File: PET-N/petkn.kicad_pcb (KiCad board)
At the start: 2 copper layers, 386.1 x 102 mm, 140 parts, among them J1 Extended_PET_keyboard_connect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, J4 AVR-ISP-6, J7 AVR-ISP-6, SW1 KP "=", SW10 KP "0", SW11 R SHIFT, SW12 ">", SW14 "]", SW15 "@", SW16 L SHIFT, SW17 KP "+", SW18 KP "2", SW2 KP ".", SW20 "?", SW21 ",", SW22 "N", SW23 "V", SW24 "X", SW25 KP "3", SW26 KP "1", SW27 RETURN, SW28 ";", SW29 "M", SW3 NC ($10), SW30 "B", SW31 "C", SW32 "Z", SW320 S LOCK, SW33 KP "*", SW34 KP "5", SW36 ":", SW37 "K", SW38 "H", SW39 "F", SW4 STOP, SW40 "S", SW41 KP "6", SW42 KP "4", SW44 "L", SW45 "J", SW46 "G", SW47 "D", SW48 "A", SW49 KP "/", SW5 "<", SW50 KP "8", SW52 "P", SW53 "I", SW54 "Y", SW55 "R", SW56 "W", SW57 KP "9", SW58 KP "7", SW59 U ARROW, SW6 SPACE, SW60 "O", SW61 "U", SW62 "T", SW63 "E", SW64 "Q", SW65 INS/DEL, SW66 UP/DOWN, SW67 NC ($0A), SW68 ")", SW69 "\", SW7 "[", SW70 "'", SW71 "$", SW72 QUOTE, SW73 LEFT/RIGHT, SW74 CLR/HOME, SW75 B ARROW, SW76 "(", SW77 "&", SW78 "%", SW79 "#", SW8 OFF/RVS, SW80 "!", SW9 KP "-", U1 LSF0204Q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

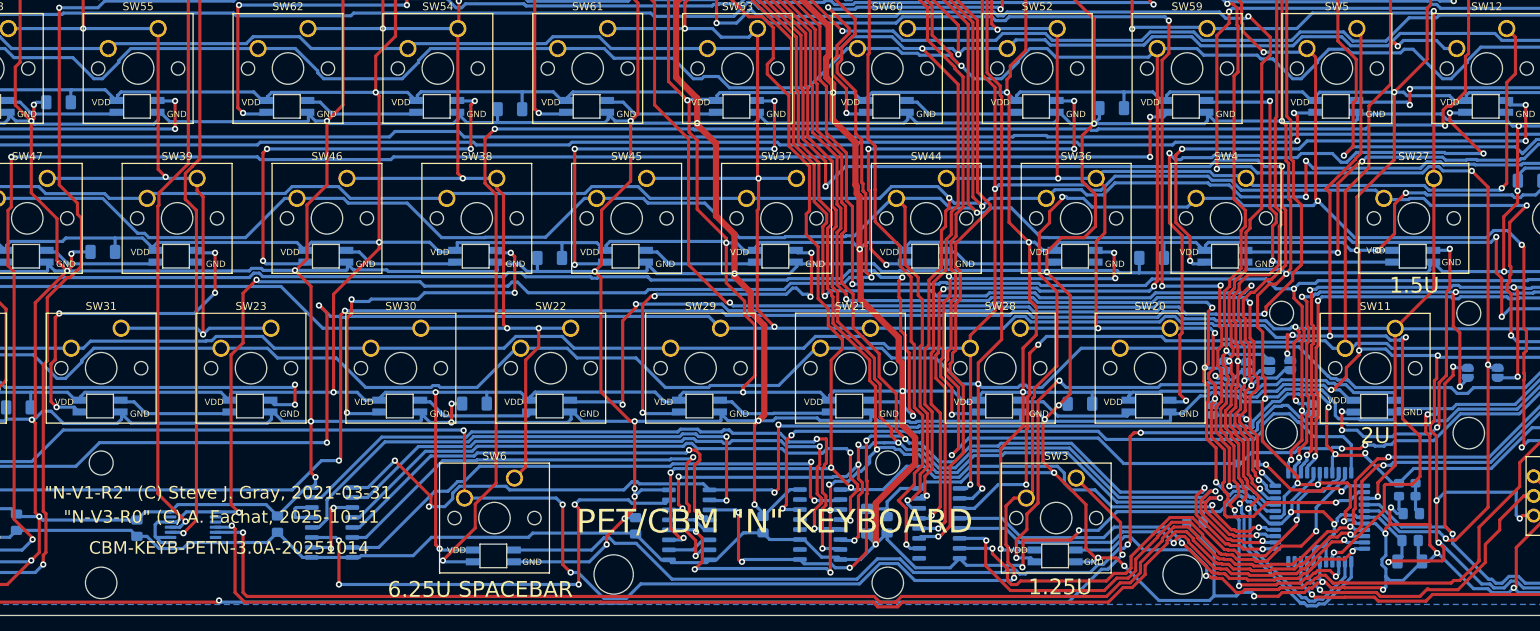
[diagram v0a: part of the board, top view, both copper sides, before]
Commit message: fix the two 3.0A issues (temporarily)
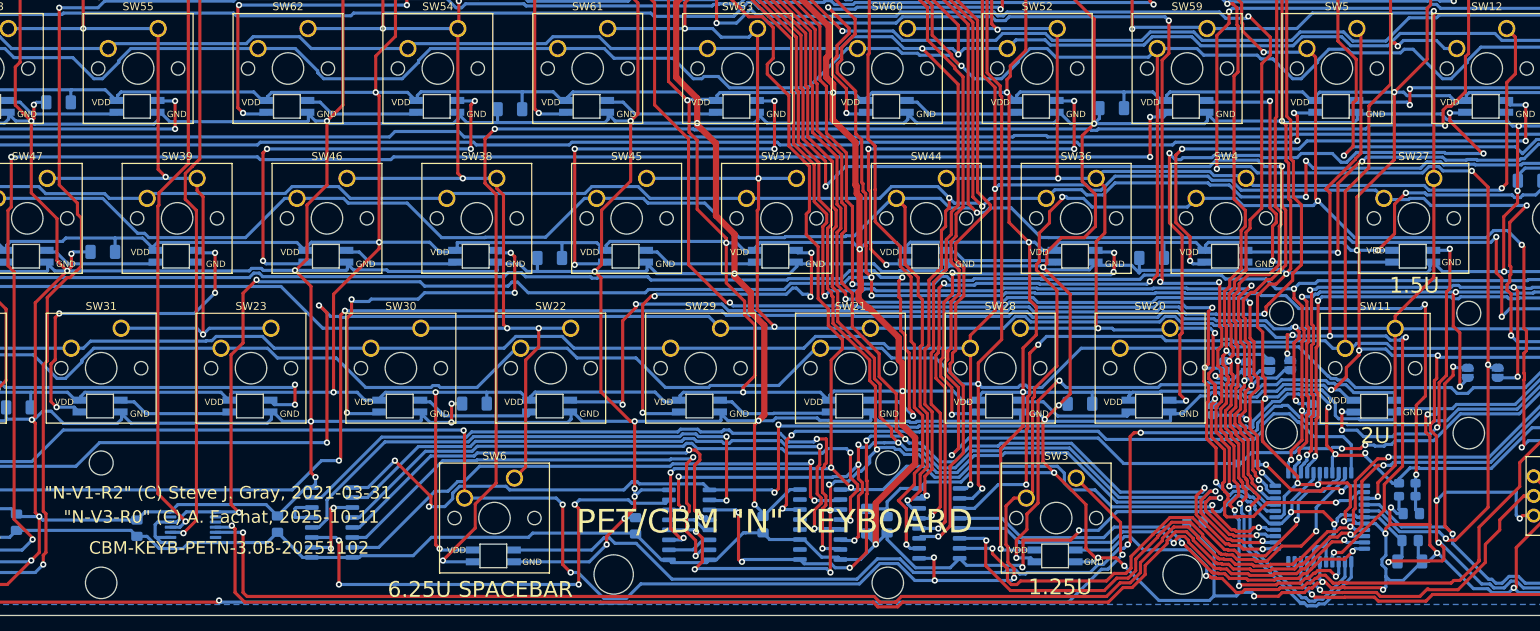
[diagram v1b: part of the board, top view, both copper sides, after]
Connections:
- C7 pad 1: V33 -> VCC33
- U7 pad 1: R0 -> R10
- Y1 pad 1: V33 -> VCC33
- Y1 pad 4: V33 -> VCC33
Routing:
- net VCC33: track 188.2 -> 289.5 mm, vias 3 -> 6
- net R10: track 592.8 -> 598.0 mm, vias 13 -> 15
- net V33: track 4.07 -> 0.00 mm
- net C4: track 464.0 -> 460.2 mm
- net GND: track 2664.5 -> 2665.8 mm
- net Net-(SW28B-DOUT): track 49.4 -> 48.6 mm
- net CC3: track 157.5 -> 156.8 mm
- net CC6: track 229.8 -> 230.4 mm
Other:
- board text added: "CBM-KEYB-PETN-3.0B-20251102"
- board text removed: "CBM-KEYB-PETN-3.0A-20251014"

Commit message: first run on r3.1
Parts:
- added D10: 1N4448, Diode_SMD:D_SOD-323_HandSoldering, B.Cu at (58.5, 73.6)
- added D11: 1N4448, Diode_SMD:D_SOD-323_HandSoldering, B.Cu at (49.0, 54.5)
- added D12: 1N4448, Diode_SMD:D_SOD-323_HandSoldering, B.Cu at (258.5, 54.5)
- added D13: 1N4448, Diode_SMD:D_SOD-323_HandSoldering, B.Cu at (30.0, 54.4)
- added D14: 1N4448, Diode_SMD:D_SOD-323_HandSoldering, B.Cu at (130.0, 111.8)
- added D15: 1N4448, Diode_SMD:D_SOD-323_HandSoldering, B.Cu at (110.9, 111.7)
- added D16: 1N4448, Diode_SMD:D_SOD-323_HandSoldering, B.Cu at (120.7, 92.7)
- added D17: 1N4448, Diode_SMD:D_SOD-323_HandSoldering, B.Cu at (101.7, 92.6)
- added D18: 1N4448, Diode_SMD:D_SOD-323_HandSoldering, B.Cu at (115.7, 73.6)
- added D19: 1N4448, Diode_SMD:D_SOD-323_HandSoldering, B.Cu at (96.7, 73.5)
- added D2: 1N4448, Diode_SMD:D_SOD-323_HandSoldering, B.Cu at (34.8, 73.5)
- added D20: 1N4448, Diode_SMD:D_SOD-323_HandSoldering, B.Cu at (106.2, 54.5)
- added D21: 1N4448, Diode_SMD:D_SOD-323_HandSoldering, B.Cu at (87.2, 54.4)
- added D22: 1N4448, Diode_SMD:D_SOD-323_HandSoldering, B.Cu at (160.9, 130.9)
- added D23: 1N4448, Diode_SMD:D_SOD-323_HandSoldering, B.Cu at (277.7, 54.6)
- added D24: 1N4448, Diode_SMD:D_SOD-323_HandSoldering, B.Cu at (168.2, 111.8)
- added D25: 1N4448, Diode_SMD:D_SOD-323_HandSoldering, B.Cu at (149.2, 111.7)
- added D26: 1N4448, Diode_SMD:D_SOD-323_HandSoldering, B.Cu at (158.7, 92.7)
- added D27: 1N4448, Diode_SMD:D_SOD-323_HandSoldering, B.Cu at (139.8, 92.8)
- added D28: 1N4448, Diode_SMD:D_SOD-323_HandSoldering, B.Cu at (153.8, 73.5)
- added D29: 1N4448, Diode_SMD:D_SOD-323_HandSoldering, B.Cu at (134.6, 73.4)
- added D3: 1N4448, Diode_SMD:D_SOD-323_HandSoldering, B.Cu at (91.8, 111.7)
- added D30: 1N4448, Diode_SMD:D_SOD-323_HandSoldering, B.Cu at (144.3, 54.6)
- added D31: 1N4448, Diode_SMD:D_SOD-323_HandSoldering, B.Cu at (125.3, 54.6)
- added D32: 1N4448, Diode_SMD:D_SOD-323_HandSoldering, B.Cu at (268.1, 73.5)
- added D33: 1N4448, Diode_SMD:D_SOD-323_HandSoldering, B.Cu at (253.8, 92.7)
- added D34: 1N4448, Diode_SMD:D_SOD-323_HandSoldering, B.Cu at (206.3, 111.7)
- added D35: 1N4448, Diode_SMD:D_SOD-323_HandSoldering, B.Cu at (187.3, 111.9)
- added D36: 1N4448, Diode_SMD:D_SOD-323_HandSoldering, B.Cu at (196.8, 92.6)
- added D37: 1N4448, Diode_SMD:D_SOD-323_HandSoldering, B.Cu at (177.8, 92.8)
- added D38: 1N4448, Diode_SMD:D_SOD-323_HandSoldering, B.Cu at (191.8, 73.5)
- added D39: 1N4448, Diode_SMD:D_SOD-323_HandSoldering, B.Cu at (172.8, 73.5)
- added D4: 1N4448, Diode_SMD:D_SOD-323_HandSoldering, B.Cu at (82.5, 92.6)
- added D40: 1N4448, Diode_SMD:D_SOD-323_HandSoldering, B.Cu at (182.5, 54.5)
- added D41: 1N4448, Diode_SMD:D_SOD-323_HandSoldering, B.Cu at (163.2, 54.5)
- added D42: 1N4448, Diode_SMD:D_SOD-323_HandSoldering, B.Cu at (287.2, 73.4)
- added D43: 1N4448, Diode_SMD:D_SOD-323_HandSoldering, B.Cu at (244.5, 111.6)
- added D44: 1N4448, Diode_SMD:D_SOD-323_HandSoldering, B.Cu at (225.2, 111.6)
- added D45: 1N4448, Diode_SMD:D_SOD-323_HandSoldering, B.Cu at (235.0, 92.8)
- added D46: 1N4448, Diode_SMD:D_SOD-323_HandSoldering, B.Cu at (215.7, 92.7)
- added D47: 1N4448, Diode_SMD:D_SOD-323_HandSoldering, B.Cu at (230.0, 73.4)
- added D48: 1N4448, Diode_SMD:D_SOD-323_HandSoldering, B.Cu at (211.0, 73.6)
- added D49: 1N4448, Diode_SMD:D_SOD-323_HandSoldering, B.Cu at (220.2, 54.6)
- added D5: 1N4448, Diode_SMD:D_SOD-323_HandSoldering, B.Cu at (77.5, 73.6)
- added D50: 1N4448, Diode_SMD:D_SOD-323_HandSoldering, B.Cu at (201.5, 54.8)
- added D51: 1N4448, Diode_SMD:D_SOD-323_HandSoldering, B.Cu at (340.7, 130.7)
- added D52: 1N4448, Diode_SMD:D_SOD-323_HandSoldering, B.Cu at (273.0, 111.8)
- added D53: 1N4448, Diode_SMD:D_SOD-323_HandSoldering, B.Cu at (321.8, 130.8)
- added D54: 1N4448, Diode_SMD:D_SOD-323_HandSoldering, B.Cu at (277.6, 92.7)
- added D55: 1N4448, Diode_SMD:D_SOD-323_HandSoldering, B.Cu at (340.9, 111.7)
- added D56: 1N4448, Diode_SMD:D_SOD-323_HandSoldering, B.Cu at (321.6, 111.6)
- added D57: 1N4448, Diode_SMD:D_SOD-323_HandSoldering, B.Cu at (340.9, 92.6)
- added D58: 1N4448, Diode_SMD:D_SOD-323_HandSoldering, B.Cu at (249.1, 73.5)
- added D59: 1N4448, Diode_SMD:D_SOD-323_HandSoldering, B.Cu at (321.6, 92.7)
- added D6: 1N4448, Diode_SMD:D_SOD-323_HandSoldering, B.Cu at (68.0, 54.5)
- added D60: 1N4448, Diode_SMD:D_SOD-323_HandSoldering, B.Cu at (239.6, 54.4)
- added D61: 1N4448, Diode_SMD:D_SOD-323_HandSoldering, B.Cu at (340.9, 73.6)
- added D62: 1N4448, Diode_SMD:D_SOD-323_HandSoldering, B.Cu at (321.6, 73.6)
- added D63: 1N4448, Diode_SMD:D_SOD-323_HandSoldering, B.Cu at (340.6, 54.5)
- added D64: 1N4448, Diode_SMD:D_SOD-323_HandSoldering, B.Cu at (321.6, 54.5)
- added D65: 1N4448, Diode_SMD:D_SOD-323_HandSoldering, B.Cu at (378.8, 130.8)
- added D66: 1N4448, Diode_SMD:D_SOD-323_HandSoldering, B.Cu at (359.8, 130.8)
- added D67: 1N4448, Diode_SMD:D_SOD-323_HandSoldering, B.Cu at (378.8, 111.7)
- added D68: 1N4448, Diode_SMD:D_SOD-323_HandSoldering, B.Cu at (359.8, 111.7)
- added D69: 1N4448, Diode_SMD:D_SOD-323_HandSoldering, B.Cu at (378.8, 92.6)
- added D7: 1N4448, Diode_SMD:D_SOD-323_HandSoldering, B.Cu at (44.3, 111.7)
- added D70: 1N4448, Diode_SMD:D_SOD-323_HandSoldering, B.Cu at (359.8, 92.6)
- added D71: 1N4448, Diode_SMD:D_SOD-323_HandSoldering, B.Cu at (378.5, 73.8)
- added D72: 1N4448, Diode_SMD:D_SOD-323_HandSoldering, B.Cu at (359.8, 73.7)
- added D73: 1N4448, Diode_SMD:D_SOD-323_HandSoldering, B.Cu at (379.0, 54.7)
- added D74: 1N4448, Diode_SMD:D_SOD-323_HandSoldering, B.Cu at (359.8, 54.6)
- added D75: 1N4448, Diode_SMD:D_SOD-323_HandSoldering, B.Cu at (39.5, 92.5)
- added D76: 1N4448, Diode_SMD:D_SOD-323_HandSoldering, B.Cu at (232.3, 130.7)
- added D77: 1N4448, Diode_SMD:D_SOD-323_HandSoldering, B.Cu at (87.3, 130.9)
- added D8: 1N4448, Diode_SMD:D_SOD-323_HandSoldering, B.Cu at (72.8, 111.7)
- added D9: 1N4448, Diode_SMD:D_SOD-323_HandSoldering, B.Cu at (63.5, 92.6)
- added R1: 2k2, Resistor_SMD:R_0603_1608Metric, B.Cu at (123.5, 130.8)
- added R2: 2k2, Resistor_SMD:R_0603_1608Metric, B.Cu at (128.5, 130.3)
- moved JC3 81.2 mm to (196.9, 68.0)
- moved JC7 81.2 mm to (222.1, 68.9)
- moved JC1 81.2 mm to (191.2, 68.1)
- moved JC2 81.2 mm to (194.0, 68.2)
- moved JC4 81.2 mm to (199.5, 68.0)
- moved JC8 81.2 mm to (225.9, 68.9)
- moved JC6 81.2 mm to (202.3, 73.5)
- moved U2 1.58 mm to (269.0, 137.2)
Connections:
- SW1 pad 2: R10 -> Net-(D65-A)
- SW10 pad 2: R9 -> Net-(D53-A)
- SW11 pad 2: R9 -> Net-(D52-A)
- SW12 pad 2: R9 -> Net-(D42-A)
- SW14 pad 2: R9 -> Net-(D23-A)
- SW15 pad 2: R9 -> Net-(D13-A)
- SW16 pad 2: R9 -> Net-(D7-A)
- SW17 pad 2: R8 -> Net-(D67-A)
- SW18 pad 2: R8 -> Net-(D55-A)
- SW2 pad 2: R10 -> Net-(D51-A)
- SW20 pad 2: R8 -> Net-(D43-A)
- SW21 pad 2: R8 -> Net-(D34-A)
- SW22 pad 2: R8 -> Net-(D24-A)
- SW23 pad 2: R8 -> Net-(D14-A)
- SW24 pad 2: R8 -> Net-(D3-A)
- SW25 pad 2: R7 -> Net-(D68-A)
- SW26 pad 2: R7 -> Net-(D56-A)
- SW27 pad 2: R7 -> Net-(D54-A)
- SW28 pad 2: R7 -> Net-(D44-A)
- SW29 pad 2: R7 -> Net-(D35-A)
- SW3 pad 2: R10 -> Net-(D76-A)
- SW30 pad 2: R7 -> Net-(D25-A)
- SW31 pad 2: R7 -> Net-(D15-A)
- SW32 pad 2: R7 -> Net-(D8-A)
- SW320 pad 2: xR9 -> Net-(D75-A)
- SW33 pad 2: R6 -> Net-(D69-A)
- SW34 pad 2: R6 -> Net-(D57-A)
- SW36 pad 2: R6 -> Net-(D45-A)
- SW37 pad 2: R6 -> Net-(D36-A)
- SW38 pad 2: R6 -> Net-(D26-A)
- SW39 pad 2: R6 -> Net-(D16-A)
- SW4 pad 2: R10 -> Net-(D33-A)
- SW40 pad 2: R6 -> Net-(D4-A)
- SW41 pad 2: R5 -> Net-(D70-A)
- SW42 pad 2: R5 -> Net-(D59-A)
- SW44 pad 2: R5 -> Net-(D46-A)
- SW45 pad 2: R5 -> Net-(D37-A)
- SW46 pad 2: R5 -> Net-(D27-A)
- SW47 pad 2: R5 -> Net-(D17-A)
- SW48 pad 2: R5 -> Net-(D9-A)
- SW49 pad 2: R4 -> Net-(D71-A)
- SW5 pad 2: R10 -> Net-(D32-A)
- SW50 pad 2: R4 -> Net-(D61-A)
- SW52 pad 2: R4 -> Net-(D47-A)
- SW53 pad 2: R4 -> Net-(D38-A)
- SW54 pad 2: R4 -> Net-(D28-A)
- SW55 pad 2: R4 -> Net-(D18-A)
- SW56 pad 2: R4 -> Net-(D5-A)
- SW57 pad 2: R3 -> Net-(D72-A)
- SW58 pad 2: R3 -> Net-(D62-A)
- SW59 pad 2: R3 -> Net-(D58-A)
- SW6 pad 2: R10 -> Net-(D22-A)
- SW60 pad 2: R3 -> Net-(D48-A)
- SW61 pad 2: R3 -> Net-(D39-A)
- SW62 pad 2: R3 -> Net-(D29-A)
- SW63 pad 2: R3 -> Net-(D19-A)
- SW64 pad 2: R3 -> Net-(D10-A)
- SW65 pad 2: R2 -> Net-(D73-A)
- SW66 pad 2: R2 -> Net-(D63-A)
- SW67 pad 2: XR67 -> Net-(D77-A)
- SW68 pad 2: R2 -> Net-(D49-A)
- SW69 pad 2: R2 -> Net-(D40-A)
- SW7 pad 2: R10 -> Net-(D12-A)
- SW70 pad 2: R2 -> Net-(D30-A)
- SW71 pad 2: R2 -> Net-(D20-A)
- SW72 pad 2: R2 -> Net-(D6-A)
- SW73 pad 2: R1 -> Net-(D74-A)
- SW74 pad 2: R1 -> Net-(D64-A)
- SW75 pad 2: R1 -> Net-(D60-A)
- SW76 pad 2: R1 -> Net-(D50-A)
- SW77 pad 2: R1 -> Net-(D41-A)
- SW78 pad 2: R1 -> Net-(D31-A)
- SW79 pad 2: R1 -> Net-(D21-A)
- SW8 pad 2: R10 -> Net-(D2-A)
- SW80 pad 2: R1 -> Net-(D11-A)
- SW9 pad 2: R9 -> Net-(D66-A)
- U7 pad 1: R10 -> R1
- U7 pad 10: R8 -> R9
- U7 pad 11: R9 -> R10
- U7 pad 2: R1 -> R2
- U7 pad 3: R2 -> R3
- U7 pad 4: R3 -> R4
- U7 pad 5: R4 -> R5
- U7 pad 6: R5 -> R6
- U7 pad 7: R6 -> R7
- U7 pad 9: R7 -> R8
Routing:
- net VCC: track 2762.8 -> 0.00 mm, vias 70 -> 0
- net GND: track 2665.8 -> 0.00 mm, vias 86 -> 0
- net R9: track 600.0 -> 0.00 mm, vias 9 -> 0
- net R10: track 598.0 -> 0.00 mm, vias 15 -> 0
- net C3: track 535.7 -> 0.00 mm, vias 12 -> 0
- net R2: track 522.4 -> 0.00 mm, vias 1 -> 0
- net R4: track 497.6 -> 0.00 mm, vias 4 -> 0
- net C1: track 493.6 -> 0.00 mm, vias 7 -> 0
- net C2: track 463.2 -> 0.00 mm, vias 5 -> 0
- net C4: track 460.2 -> 0.00 mm, vias 11 -> 0
- net R3: track 458.3 -> 0.00 mm, vias 4 -> 0
- net R5: track 452.2 -> 0.00 mm, vias 6 -> 0
- net C6: track 448.3 -> 0.00 mm, vias 9 -> 0
- net R1: track 435.6 -> 0.00 mm, vias 4 -> 0
- net R7: track 416.8 -> 0.00 mm, vias 5 -> 0
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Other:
- board text added: "CBM-KEYB-PETN-3.1A-20260130 (C) Steve J. Gray, André Fachat"
- board text removed: ""N-V1-R2" (C) Steve J. Gray, 2021-03-31"
- board text removed: "CBM-KEYB-PETN-3.0B-20251102"
- board text removed: "{dblquote}N-V3-R0{dblquote} (C) A. Fachat, 2025-10-11"

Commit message: working on new layout
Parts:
- added D78: 1N4448, Diode_SMD:D_SOD-323_HandSoldering, B.Cu at (297.7, 115.5)
- added D79: 1N4448, Diode_SMD:D_SOD-323_HandSoldering, B.Cu at (300.8, 79.1)
- added JP5: SolderJumper_2_Bridged, Jumper:SolderJumper-2_P1.3mm_Open_RoundedPad1.0x1.5mm, B.Cu at (290.2, 114.5)
- added R3: 10k, Resistor_SMD:R_0603_1608Metric, B.Cu at (290.3, 117.6)
- added U9: 74HCT00, Package_SO:SOIC-14_3.9x8.7mm_P1.27mm, B.Cu at (305.0, 114.5)
- moved D1 38.1 mm to (294.9, 115.4), turned to 90 degrees
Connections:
- net Net-(D1-K) renamed /RESOUT
- J4 pad 5: Net-(J4-~{RST}) -> Net-(D78-K)
- J7 pad 5: cR1 -> Net-(D79-K)
- U2 pad 4: Net-(J4-~{RST}) -> /RESSCAN
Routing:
- net C4: track 0.00 -> 337.9 mm, vias 0 -> 1
- net C3: track 0.00 -> 299.6 mm, vias 0 -> 2
- net L7: track 0.00 -> 293.1 mm, vias 0 -> 2
- net C2: track 0.00 -> 280.8 mm, vias 0 -> 1
- net R9: track 0.00 -> 271.8 mm, vias 0 -> 3
- net Net-(SW320B-DIN): track 0.00 -> 240.7 mm, vias 0 -> 2
- net Net-(SW15B-DIN): track 0.00 -> 226.0 mm, vias 0 -> 2
- net C1: track 0.00 -> 221.8 mm, vias 0 -> 1
- net Net-(SW21B-DIN): track 0.00 -> 191.4 mm, vias 0 -> 2
- net VCC: track 0.00 -> 185.4 mm, vias 0 -> 10
- net Net-(SW15B-DOUT): track 0.00 -> 178.3 mm, vias 0 -> 2
- net R2: track 0.00 -> 138.8 mm, vias 0 -> 4
- net C5: track 0.00 -> 134.5 mm
- net C8: track 0.00 -> 95.3 mm
- net C7: track 0.00 -> 95.3 mm
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
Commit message: layout work
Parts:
- added D80: 1N4448, Diode_SMD:D_SOD-323_HandSoldering, B.Cu at (312.1, 117.0)
- added D81: 1N4448, Diode_SMD:D_SOD-323_HandSoldering, B.Cu at (312.7, 112.2)
- added R4: 10k, Resistor_SMD:R_0603_1608Metric, B.Cu at (314.7, 116.3)
- added R5: 10k, Resistor_SMD:R_0603_1608Metric, B.Cu at (314.7, 112.2)
- moved JC1 1.88 mm to (191.2, 69.9)
- moved JC2 1.88 mm to (194.0, 70.0)
- moved JC4 1.88 mm to (199.5, 69.8), turned to -90 degrees
- moved JC3 1.88 mm to (196.8, 69.9)
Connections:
- D78 pad 2: /RESSCAN -> Net-(D78-A)
- U2 pad 4: /RESSCAN -> Net-(D78-A)
- U9 pad 8: /RES -> /RESLED
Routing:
- net VCC: track 185.4 -> 2232.1 mm, vias 10 -> 130
- net GND: track 0.00 -> 1605.8 mm, vias 0 -> 95
- net R4: track 87.9 -> 402.9 mm, vias 3 -> 10
- net R1: track 44.7 -> 339.0 mm, vias 3 -> 10
- net R2: track 138.8 -> 430.7 mm, vias 4 -> 9
- net C6: track 25.5 -> 227.8 mm
- net XC3: track 0.00 -> 196.6 mm, vias 0 -> 1
- net LVSCL: track 0.00 -> 180.2 mm, vias 0 -> 2
- net LVSDA: track 0.00 -> 177.2 mm, vias 0 -> 2
- net CC1: track 0.66 -> 168.1 mm, vias 0 -> 4
- net R3: track 0.00 -> 164.9 mm, vias 0 -> 3
- net cR2: track 0.00 -> 163.7 mm, vias 0 -> 2
- net R5: track 0.00 -> 162.0 mm, vias 0 -> 5
- net cR1: track 0.00 -> 150.6 mm, vias 0 -> 2
- net CC6: track 0.00 -> 149.2 mm, vias 0 -> 2
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
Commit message: layout work
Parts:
- moved R1 11.4 mm to (133.2, 136.8), turned to 90 degrees
- moved R2 7.04 mm to (131.2, 136.8), turned to 90 degrees
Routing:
- net R3: track 164.9 -> 433.8 mm, vias 3 -> 11
- net R8: track 0.00 -> 265.0 mm, vias 0 -> 7
- net R7: track 0.00 -> 264.4 mm, vias 0 -> 6
- net R6: track 0.00 -> 264.3 mm, vias 0 -> 8
- net R10: track 183.0 -> 438.2 mm, vias 4 -> 12
- net Net-(SW67B-DOUT): track 0.00 -> 248.2 mm, vias 0 -> 2
- net Net-(SW59B-DOUT): track 0.00 -> 220.3 mm, vias 0 -> 2
- net L5: track 0.00 -> 213.8 mm, vias 0 -> 2
- net Net-(SW14B-DIN): track 0.00 -> 213.2 mm, vias 0 -> 4
- net SDA: track 0.00 -> 176.4 mm, vias 0 -> 2
- net SCL: track 0.00 -> 172.6 mm, vias 0 -> 2
- net Net-(SW14B-DOUT): track 0.00 -> 157.0 mm, vias 0 -> 2
- net C3: track 301.4 -> 456.5 mm, vias 3 -> 5
- net Net-(SW15B-DIN): track 80.4 -> 225.9 mm
- net VCC33: track 67.8 -> 205.5 mm, vias 1 -> 2
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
